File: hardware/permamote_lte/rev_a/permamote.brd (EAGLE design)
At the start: 27 x 60 mm, 106 parts, among them IC1 NRF9160, J1 TC2030-JLINK-NL, J2 U.FL-R-SMT, J3 NANO_SIM, J4 U.FL-R-SMT, Q1 PMDXB950UPEL, Q10 PMDXB950UPEL, Q2 PMDXB950UPEL, Q3 PMDXB950UPEL, Q4 PMDXB950UPEL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

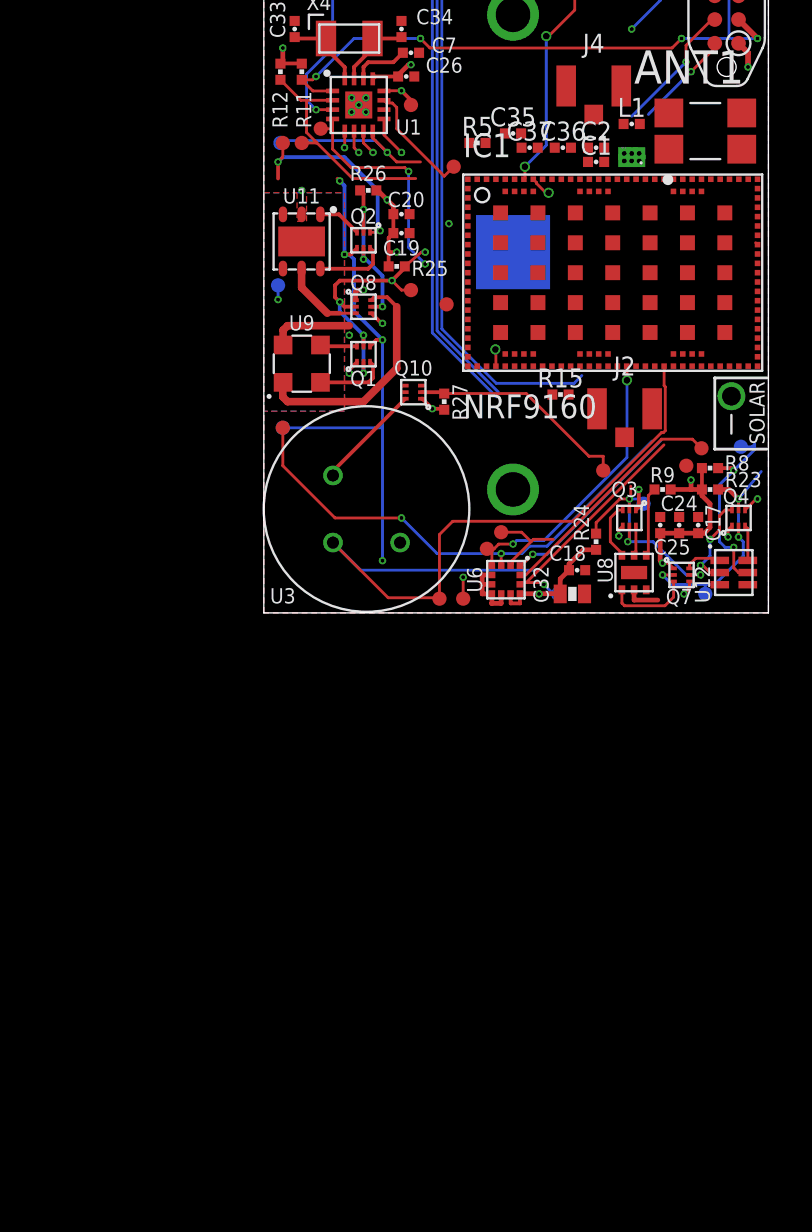
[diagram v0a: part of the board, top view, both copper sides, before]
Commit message: made revisions from schematic review
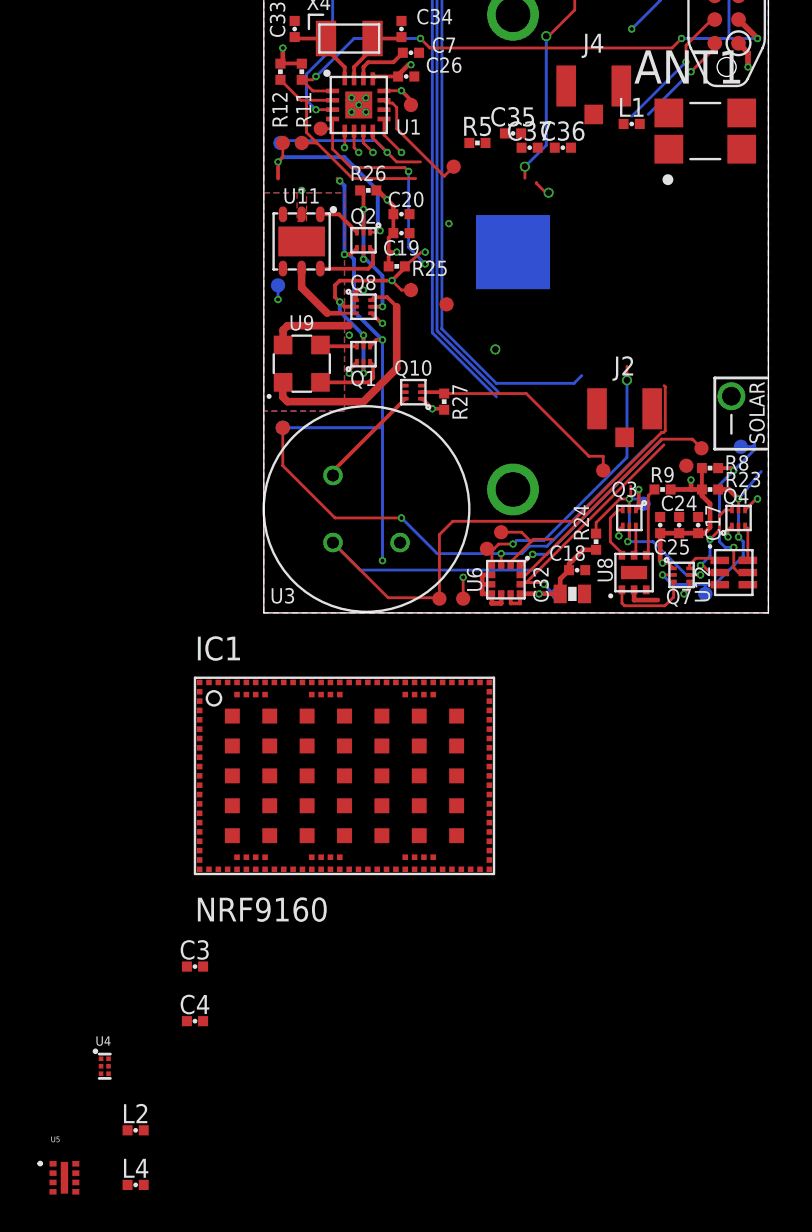
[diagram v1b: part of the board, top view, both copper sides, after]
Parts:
- removed C1: 5.1pF, passives:0402_CAP
- removed C2: .8pF, passives:0402_CAP
- removed R15: 50, passives:0402_RES
- removed U$1: BGA725L6, permamote:BGA725L6
- added C3, C4: (no value), passives:0402_CAP
- added L2: 5.1nH, passives:0402_CAP
- added L4: 1.8nH, passives:0402_CAP
- added U4: BGA725L6, Particle:LNA-TSLP-6-2-ORIG
- added U5: TPD3F303DPVR, TPD3F303:DPV8_1P7X0P4
- moved IC1 30.5 mm to (-3.68, -14.0)
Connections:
- removed net N$30: IC1.ANT, J2.SIG, R15.2
- removed net N$36: IC1.SIM_IO
- removed net N$37: IC1.SIM_CLK
- new net N$11: C4.2, J2.SIG
- new net N$40: J3.C2
- new net N$6: U4.6
- new net N$7: C37.1, IC1.VDD_GPIO
- new net N$8: C3.2, C4.1
- new net N$9: C3.1, IC1.ANT
- new net SIM_CLK2: J3.C3, U5.2
- new net SIM_IO2: J3.C7, U5.3
- new net SIM_RST2: U5.1
- net !LT_INT: now also IC1.P0.02; no longer IC1.P0.19
- net !RST: now also IC1.NRESET; no longer IC1.P0.26
- net GND: now also L4.1, U4.1, U4.4; no longer C1.2, R15.1, U$1.1, U$1.4
- net LBST: no longer IC1.P0.29
- net LED_GREEN: now also IC1.P0.19
- net N$1: now also U4.3; no longer U$1.3
- net N$2: now also U4.5; no longer U$1.5
- net N$3: now also IC1.SIM_DET; no longer U$1.6
- net N$4: now also L2.1, L4.2; no longer C2.1
- net N$5: now also L2.2; no longer C1.1, C2.2
- net SIM_1V8: now also U5.5
- net SIM_CLK: now also IC1.SIM_CLK, U5.7; no longer J3.C3
- net SIM_IO: now also IC1.SIM_IO, U5.6; no longer J3.C7
- net SIM_RST: now also U5.8; no longer J3.C2
- net SW: no longer IC1.P0.02
- net VCC: now also U4.2; no longer C37.1, IC1.VDD_GPIO, U$1.2
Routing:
- net PIR_OUT: track 39.9 -> 38.8 mm
- net VSOL: track 48.1 -> 47.2 mm

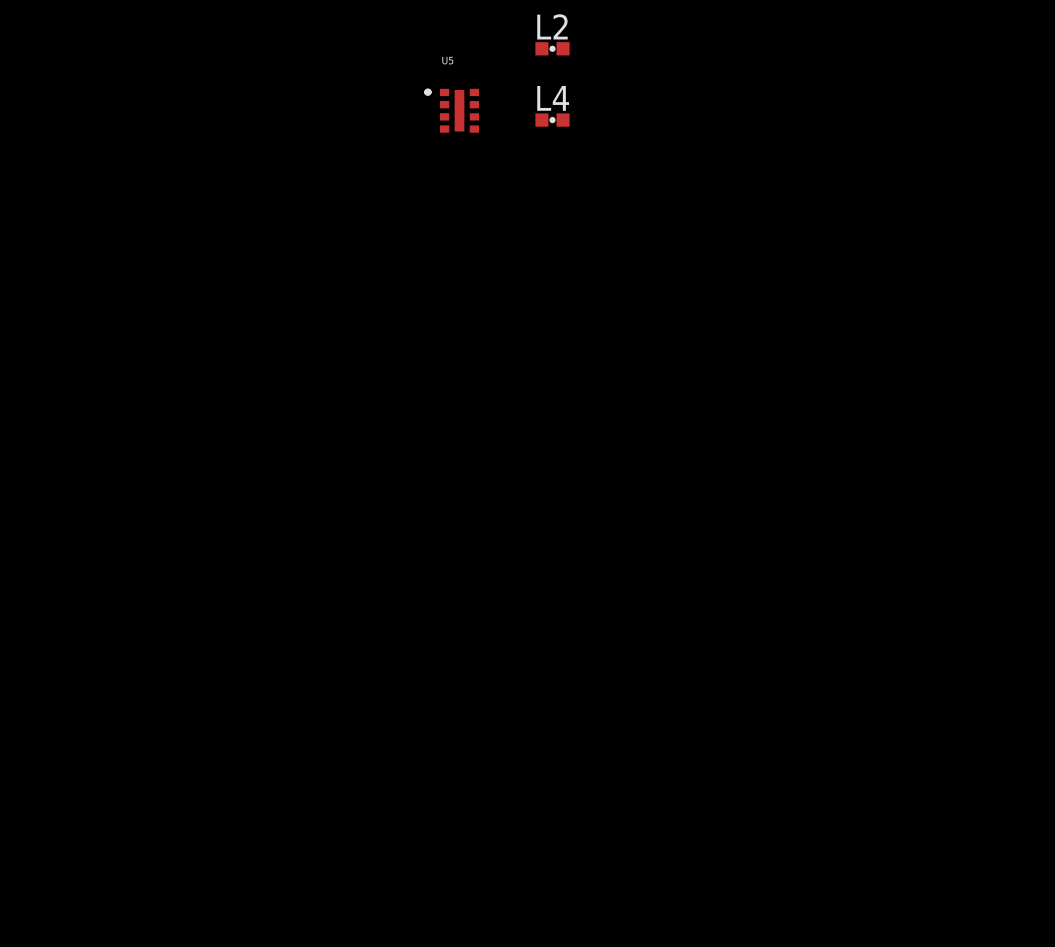
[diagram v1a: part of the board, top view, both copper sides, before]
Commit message: added sd card
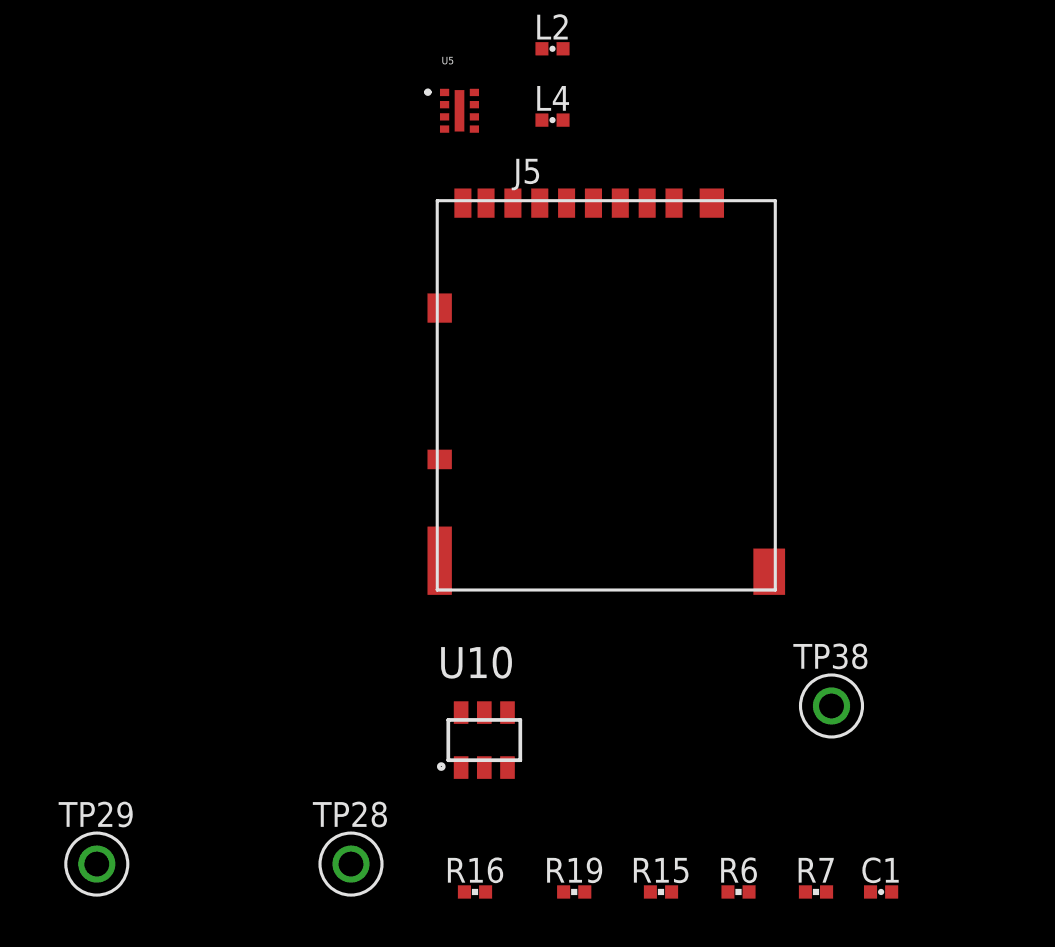
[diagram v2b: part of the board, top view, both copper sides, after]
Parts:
- added C1: 4.7uF, passives:0402_CAP
- added J5: DM3AT-SF-PEJM5, connector:DM3AT-SF-PEJM5
- added R15, R6, R7: 10k, passives:0402_RES
- added R16, R19: 100k, passives:0402_RES
- added TP28, TP29, TP38: TEST_POINT_0.040IN, headers:TESTPOINT_0.040IN
- added U10: SIP32510, chips:TSOT23-6
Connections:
- new net !SD_CS: IC1.P0.26, J5.2, R6.1
- new net !SD_DETECT: IC1.P0.27, J5.A, R16.1, TP38.TESTPOINT
- new net +3V3: R19.2, U10.5, U10.6
- new net N$13: C1.1, J5.4, R15.2, R16.2, R6.2, R7.2, U10.1, U10.2
- new net SD_ENABLE: IC1.P0.28, R19.1, U10.3
- net !CLR_INT: now also IC1.P0.29; no longer IC1.P0.28
- net !LT_EN: now also IC1.P0.09; no longer IC1.P0.27
- net !RTC_IRQ3: no longer IC1.P0.09
- net GND: now also C1.2, J5.6, J5.B, J5.MOUNT0, J5.MOUNT1, J5.MOUNT2, J5.MOUNT3, U10.4
- net MISO: now also J5.7, R15.1
- net MOSI: now also J5.3, R7.1
- net SCK: now also J5.5
- net SIM_IO2: now also TP28.TESTPOINT
- net SIM_RST2: now also TP29.TESTPOINT

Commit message: layout
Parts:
- moved TP29 103.1 mm to (19.3, 31.8)
- moved TP28 102.7 mm to (19.3, 35.7)
- moved R16 93.3 mm to (2.67, 30.2)
- moved R19 93.1 mm to (5.08, 30.2)
- moved R15 93.0 mm to (7.24, 30.2), turned to 180 degrees
- moved R6 92.9 mm to (9.78, 30.2)
- moved R7 92.9 mm to (12.7, 30.2)
- moved C1 92.9 mm to (15.2, 30.2)
- moved L4 90.6 mm to (7.87, 58.8), turned to 180 degrees
- moved L2 85.8 mm to (7.49, 56.9), turned to 270 degrees
- moved U10 83.9 mm to (7.24, 26.2), turned to 270 degrees
- moved U4 82.9 mm to (16.5, 54.7)
- moved TP38 81.0 mm to (3.56, 26.4)
- moved J5 79.9 mm to (18.8, 42.3), flipped to the bottom, turned to 180 degrees
- moved C4 77.5 mm to (7.37, 54.9), turned to 180 degrees
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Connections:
- removed net DBG_RX: IC1.P0.30
- removed net DBG_TX: IC1.P0.31
- net !LT_EN: now also IC1.P0.30; no longer IC1.P0.09
- net !RTC_IRQ3: now also IC1.P0.09
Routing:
- net LED_GREEN: track 46.4 -> 0.00 mm, vias 1 -> 0
- net LED_RED: track 49.6 -> 3.63 mm
- net SCL: track 65.0 -> 21.1 mm, vias 6 -> 5
- net LED_BLUE: track 46.4 -> 5.18 mm
- net VSEC: track 41.3 -> 0.55 mm, vias 1 -> 0
- net !RTC_EXTR: track 40.1 -> 0.18 mm, vias 2 -> 0
- net VSOL: track 47.2 -> 12.3 mm, vias 1 -> 0
- net MOSI: track 43.5 -> 9.00 mm, vias 3 -> 2
- net VBAT: track 44.7 -> 11.0 mm
- net SCK: track 42.1 -> 8.80 mm
- net PIR_OUT: track 38.8 -> 6.35 mm
- net VCC: track 67.2 -> 35.0 mm, vias 21 -> 14
- net !RST: track 36.8 -> 9.88 mm, vias 4 -> 2
- net VBAT_OK: track 28.7 -> 3.18 mm
- net SW: track 22.2 -> 0.00 mm, vias 3 -> 0
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- removed copper zone on layer 15, net VBAT
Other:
- board text removed: "CR123A PACK +"

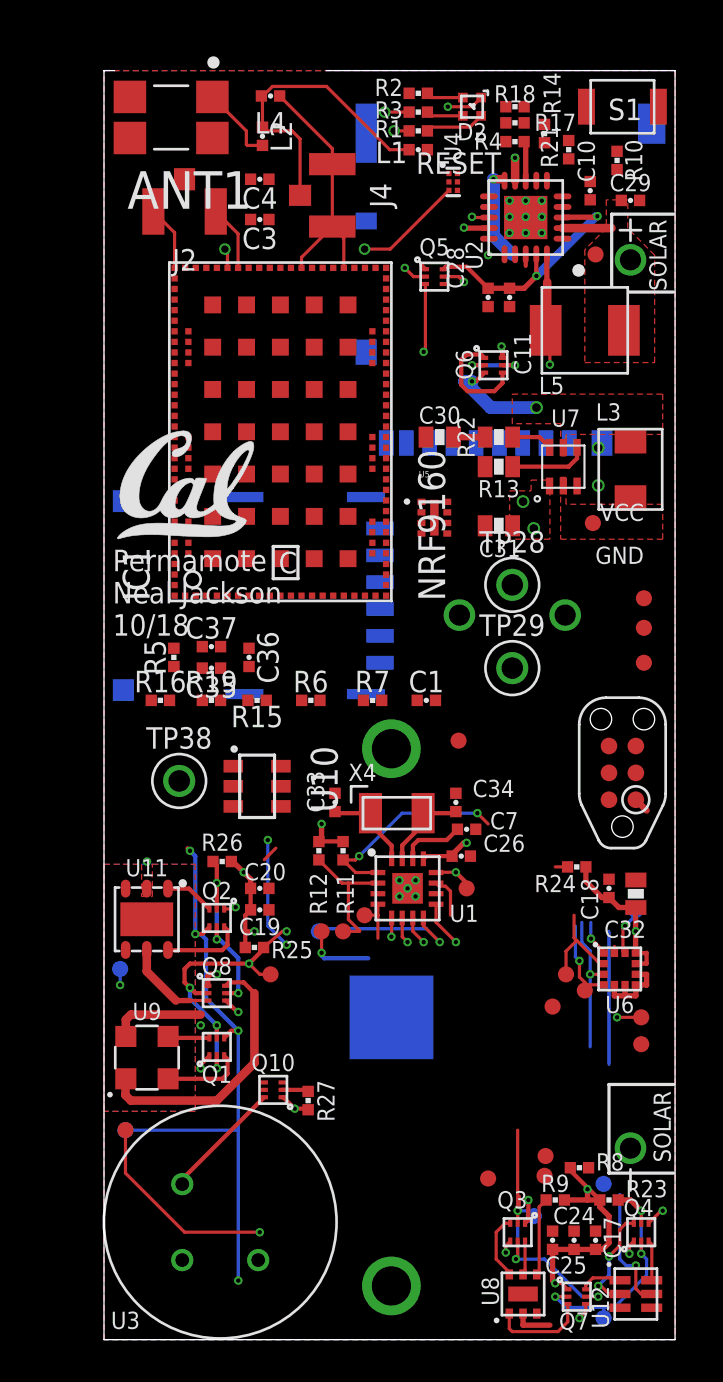
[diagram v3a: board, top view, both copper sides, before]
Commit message: routed everything except confused about ground and vcc
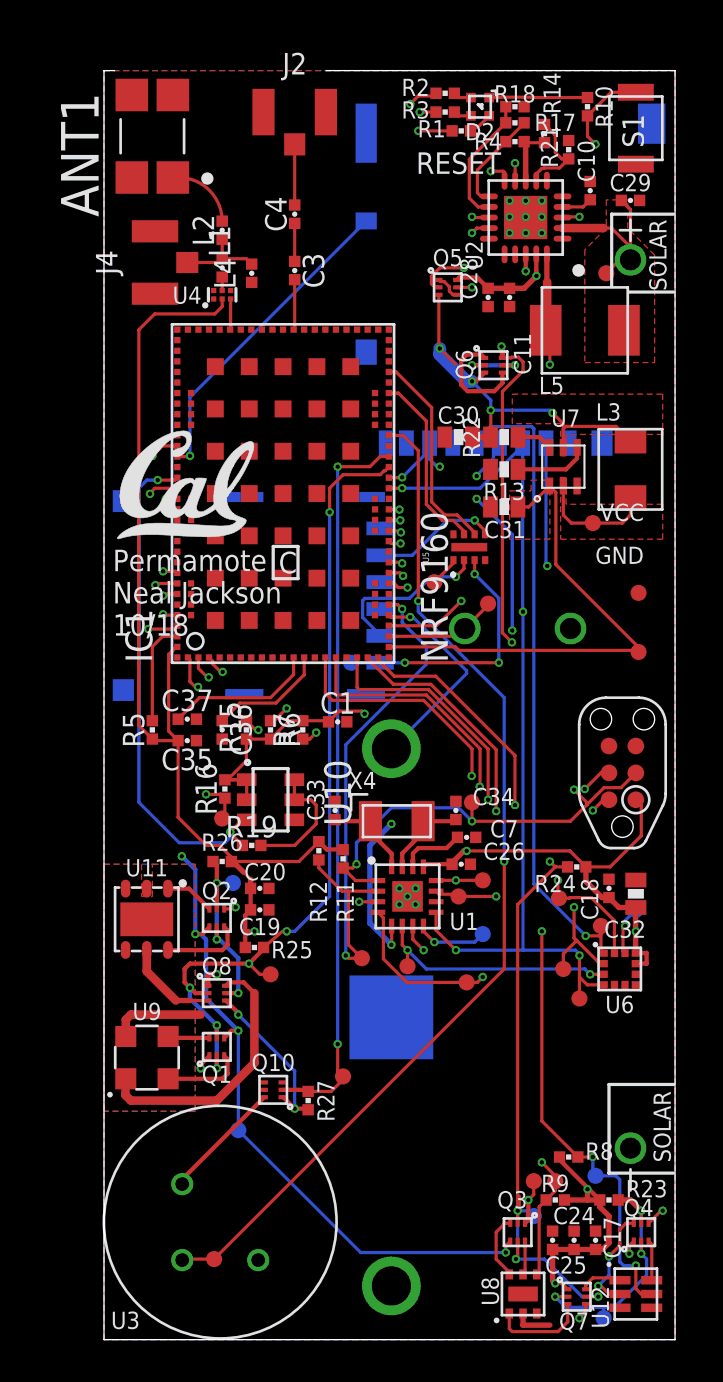
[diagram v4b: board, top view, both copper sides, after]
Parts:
- removed TP28, TP29, TP38: TEST_POINT_0.040IN, headers:TESTPOINT_0.040IN
- added TP30, TP31, TP32: TEST-POINT, headers:PAD.03X.03
- moved TP22 22.6 mm to (5.21, 3.81)
- moved TP2 15.5 mm to (20.3, 7.49)
- moved TP4 15.4 mm to (14.4, 17.7)
- moved TP18 12.2 mm to (21.5, 20.9)
- moved U4 12.2 mm to (5.59, 49.4), turned to 90 degrees
- moved L1 10.8 mm to (5.59, 50.7), turned to 90 degrees
- moved TP17 10.5 mm to (17.4, 25.4)
- moved J4 8.96 mm to (2.41, 50.9), turned to 90 degrees
- moved L4 8.43 mm to (6.99, 50.4), turned to 90 degrees
- moved TP11 8.39 mm to (11.3, 12.4)
- moved TP15 7.75 mm to (17.9, 19.2)
- moved R19 7.12 mm to (6.99, 23.4)
- moved J2 7.01 mm to (9.02, 58.0), turned to 0 degrees
- moved TP13 6.85 mm to (16.8, 21.0)
- moved TP12 6.71 mm to (6.10, 21.6)
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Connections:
- net !SD_DETECT: now also TP32.P$1; no longer TP38.TESTPOINT
- net MISO: now also IC1.P0.22; no longer IC1.P0.21
- net MOSI: now also IC1.P0.21; no longer IC1.P0.22
- net SIM_IO2: now also TP31.P$1; no longer TP28.TESTPOINT
- net SIM_RST2: now also TP30.P$1; no longer TP29.TESTPOINT
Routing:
- net VCC: track 35.0 -> 119.5 mm, vias 14 -> 9
- net VBAT: track 11.0 -> 67.2 mm, vias 3 -> 6
- net SCK: track 8.80 -> 64.3 mm
- net !CLR_INT: track 6.10 -> 58.8 mm, vias 1 -> 4
- net MOSI: track 9.00 -> 56.1 mm, vias 2 -> 5
- net !LT_EN: track 15.0 -> 62.0 mm, vias 3 -> 5
- net !RTC_EXTR: track 0.18 -> 45.6 mm, vias 0 -> 2
- net !SD_CS: track 0.00 -> 43.1 mm, vias 0 -> 3
- net PIR_OUT: track 6.35 -> 48.9 mm, vias 0 -> 2
- net !LT_INT: track 3.70 -> 41.8 mm, vias 0 -> 2
- net !CLR_EN: track 11.9 -> 47.8 mm, vias 3 -> 4
- net SCL: track 21.1 -> 56.2 mm
- net !SD_DETECT: track 0.00 -> 35.0 mm, vias 0 -> 2
- net !PIR_EN: track 1.26 -> 34.8 mm, vias 0 -> 2
- net N$13: track 0.00 -> 30.1 mm, vias 0 -> 4
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
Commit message: more routing fixes
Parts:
- removed C33, C34: DNP, passives:0402_CAP
- moved TP22 17.9 mm to (18.9, 15.2)
- moved TP1 13.5 mm to (18.0, 3.05)
- moved C37 3.77 mm to (7.11, 31.4), turned to 180 degrees
- moved TP10 2.37 mm to (22.6, 5.21)
- moved C36 2.34 mm to (7.11, 30.6), turned to 180 degrees
- moved TP30 1.94 mm to (17.5, 35.4), flipped to the bottom
- moved C3 1.91 mm to (9.02, 52.5)
- moved C35 1.78 mm to (4.06, 30.1)
- moved R5 1.65 mm to (2.29, 30.5)
- moved C4 1.40 mm to (9.02, 54.6)
- moved TP20 1.17 mm to (24.4, 7.49)
- moved L4 1.09 mm to (7.62, 51.3), turned to 180 degrees
- moved R15 1.05 mm to (6.48, 27.8)
- moved R7 1.05 mm to (9.14, 27.8)
- moved R6 1.02 mm to (8.00, 27.8)
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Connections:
- removed net N$26: C33.1, U1.16, X4.1
- removed net N$27: C34.1, U1.15, X4.2
- net GND: now also U1.15, U1.16, X4.1, X4.2; no longer C33.2, C34.2
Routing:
- net GND: track 6.49 -> 41.5 mm, vias 14 -> 75
- net VCC: track 119.5 -> 96.0 mm, vias 9 -> 17
- net N$7: track 7.14 -> 2.04 mm
- net N$27: track 4.32 -> 0.00 mm
- net N$26: track 4.28 -> 0.00 mm
- net N$40: track 0.00 -> 3.45 mm
- net VSOL: track 33.1 -> 36.0 mm
- net !LT_EN: track 62.0 -> 64.5 mm
- net N$29: track 5.60 -> 3.08 mm
- net N$9: track 2.38 -> 4.29 mm
- net PIR_OUT: track 48.9 -> 50.7 mm
- net !SD_CS: track 43.1 -> 44.8 mm
- net !HUM_EN: track 25.3 -> 23.6 mm
- net N$28: track 4.89 -> 3.24 mm
- net N$11: track 2.87 -> 1.47 mm
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- added copper zone on layer 1, net N$16
- added copper zone on layer 2, net N$24
- added copper zone on layer 15, net N$26
- added copper zone on layer 16, net N$27
- added copper zone on layer 1, net N$30
- added copper zone on layer 2, net N$35
- added copper zone on layer 15, net N$36
- added copper zone on layer 16, net N$37
- added copper zone on layer 1, net N$38
- added copper zone on layer 2, net N$39
- added copper zone on layer 15, net N$43
- added copper zone on layer 16, net N$44
